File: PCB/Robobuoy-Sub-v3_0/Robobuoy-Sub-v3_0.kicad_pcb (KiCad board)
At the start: 2 copper layers, 141 parts, among them J201 Prog, J202 ESC_BB, J301 CHRG/DATA, J302 ESC_SB, J303 ESC_BB, J304 ESC_PWR_SB, J305 ESC_PWR_BB, J306 ACCU2, J307 ACCU2, Q201 MMBT3904, Q202 MMBT5401, Q203 MMBT5401, Q204 MMBT3904, Q205 AO3400A, Q301 AO3400A, Q302 AO3401A, Q303 AO3401A, Q304 AO3400A, Q305 AO3400A, Q306 HYG025N04NA1C2, Q307 HYG025N04NA1C2, SW201 ~{RESET}, SW202 MODE, SW301 On/Off, U201 LM1117S-3.3, U202 ESP32-WROOM-32E_(visible_peri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, U203 LSM303AGRTR, U301 SN74LV1T34DBV, U302 SN74LV1T34DBV, U303 LMR16020PDDA

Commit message: PCB changes
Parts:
- removed C225, C316: 100n, A_Device:C_0603
- removed C314: 100u/10V, Capacitor_SMD:C_1210_3225Metric
- removed C318: 4.7uF/10V, Capacitor_SMD:C_1206_3216Metric
- removed J307: ACCU2, A_Connector:AMASS_XT60IPW-M_1x03_P7.20mm_Horizontal
- removed Q307: HYG025N04NA1C2, Package_DFN_QFN:PQFN-8-EP_6x5mm_P1.27mm_Generic
- added H202: MountingHole, MountingHole:MountingHole_3.2mm_M3, F.Cu at (164.4, -60.3)
- added H203: MountingHole, MountingHole:MountingHole_3.2mm_M3, F.Cu at (164.4, -52.4)
- added H204: MountingHole, MountingHole:MountingHole_3.2mm_M3, F.Cu at (162.5, -74.5)
- added J203: ESC_BB, Connector_JST:JST_XH_B3B-XH-A_1x03_P2.50mm_Vertical, F.Cu at (128.1, -24.4)
- added Q308: AON6407-MS, Package_DFN_QFN:AO_DFN-8-1EP_5.55x5.2mm_P1.27mm_EP4.12x4.6mm, F.Cu at (31.4, 42.0)
- added R214: 100, A_Device:R_0603, F.Cu at (168.4, -77.3)
- C216, C218: value 1n -> 10n
- C217: value 10n -> 1n
- C219, C221: value 10n -> 100n
- C220: value 100n -> 10n
- C222: value 100n -> 100u/10V; footprint A_Device:C_0603 -> Capacitor_SMD:C_1210_3225Metric
- C223: value 100u/10V -> 1n; footprint Capacitor_SMD:C_1210_3225Metric -> A_Device:C_0603
- C224: value 1n -> 100n
- C308, C309: value 10u/25V -> 100n; footprint A_Device:C_0805 -> A_Device:C_0603
- C312: value 100n -> 1n
- C313: value 1n -> 100u/10V; footprint A_Device:C_0603 -> Capacitor_SMD:C_1210_3225Metric
- C315: value 100u/10V -> 100n; footprint Capacitor_SMD:C_1210_3225Metric -> A_Device:C_0603
- C317: value 100n -> 4.7uF/10V; footprint A_Device:C_0603 -> Capacitor_SMD:C_1206_3216Metric
- J202: value ESC_BB -> I2C; footprint Connector_JST:JST_XH_B3B-XH-A_1x03_P2.50mm_Vertical -> Connector_JST:JST_XH_B4B-XH-A_1x04_P2.50mm_Vertical
- J301: footprint A_Connector:AMASS_XT60IPW-M_1x03_P5.50mm_Vertical -> A_Connector:RoundWire_1x03_P5.50mm_Vertical
- J304, J305: footprint A_Connector:AMASS_XT60PW-F_1x02_P7.20mm_Horizontal -> Connector_AMASS:AMASS_XT30U-M_1x02_P5.0mm_Vertical
- J306: footprint A_Connector:AMASS_XT60IPW-M_1x03_P7.20mm_Horizontal -> Connector_AMASS:AMASS_XT30U-M_1x02_P5.0mm_Vertical
- Q306: value HYG025N04NA1C2 -> AON6407-MS; footprint Package_DFN_QFN:PQFN-8-EP_6x5mm_P1.27mm_Generic -> Package_DFN_QFN:AO_DFN-8-1EP_5.55x5.2mm_P1.27mm_EP4.12x4.6mm
- R208: value 100 -> 10K
- R209: value 10K -> 100
- R210: value 2.2k -> 10K
- R212: value 100 -> 2.2k
- moved C203 103.0 mm to (130.7, -73.9)
- moved C216 103.0 mm to (134.5, -73.9)
- moved C307 103.0 mm to (73.5, -73.9)
- moved R201 103.0 mm to (138.3, -73.9)
- moved R210 103.0 mm to (142.1, -73.9)
- moved R302 103.0 mm to (77.2, -73.9)
- moved TP302 103.0 mm to (63.2, -27.6)
- moved BZ201 103.0 mm to (115.2, -43.8)
- moved C201 103.0 mm to (130.7, -78.7)
- moved C202 103.0 mm to (130.7, -76.3)
- moved C204 103.0 mm to (130.7, -71.5)
- moved C205 103.0 mm to (133.2, -48.7)
- moved C206 103.0 mm to (133.2, -44.5)
- moved C207 103.0 mm to (130.7, -69.1)
- moved C208 103.0 mm to (133.2, -40.2)
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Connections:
- C216 pad 1: GND -> SWITCH
- C216 pad 2: /CPU/VSAMP -> +3.3V
- C217 pad 1: SWITCH -> GND
- C219 pad 1: GND -> +3.3V
- C219 pad 2: +3.3V -> GND
- C220 pad 1: +3.3V -> GND
- C220 pad 2: GND -> Net-(U203-VDD)
- C221 pad 1: GND -> Net-(U203-C1)
- C221 pad 2: Net-(U203-VDD) -> GND
- C222 pad 1: Net-(U203-C1) -> Net-(U203-VDD)
- C223 pad 1: Net-(U203-VDD) -> GND
- C223 pad 2: GND -> Net-(U203-VDD)
- C224 pad 1: GND -> Net-(U203-VDD)
- C224 pad 2: Net-(U203-VDD) -> GND
- C309 pad 1: Net-(D306-K) -> Net-(J302-Pin_2)
- C310 pad 1: Net-(J302-Pin_2) -> Net-(J303-Pin_2)
- C311 pad 1: Net-(J303-Pin_2) -> /Robobuoy-Sub-PSU-v3_0/buck_sw
- C311 pad 2: GND -> Net-(U303-BOOT)
- C312 pad 1: Net-(D307-K) -> +5V
- C312 pad 2: Net-(U303-BOOT) -> GND
- D307 pad 1: Net-(D307-K) -> /Robobuoy-Sub-PSU-v3_0/buck_sw
- J202 pad 1: +5V -> /CPU/SCL
- J202 pad 2: Net-(J202-Pin_2) -> /CPU/SDA
- J202 pad 3: GND -> +5V
- L301 pad 1: Net-(D307-K) -> /Robobuoy-Sub-PSU-v3_0/buck_sw
- Q306 pad 5: Net-(J304-Pin_2) -> Net-(J305-Pin_2)
- R208 pad 1: Net-(Q205-G) -> RX_SUB
- R208 pad 2: BUZZER -> +3.3V
- R209 pad 1: +3.3V -> Net-(Q205-G)
- R209 pad 2: SWITCH -> BUZZER
- R210 pad 2: Net-(U202-SDA/GPIO21) -> SWITCH
- R211 pad 2: Net-(U202-SCL/GPIO22) -> /CPU/SDA
- R212 pad 1: Net-(D202-DIN) -> +3.3V
- R212 pad 2: LEDS -> /CPU/SCL
- R213 pad 1: Net-(J202-Pin_2) -> Net-(D202-DIN)
- R213 pad 2: Net-(D204-DOUT) -> LEDS
- R325 pad 2: Net-(Q306-G) -> Net-(Q308-G)
- R326 pad 2: Net-(Q307-G) -> Net-(Q306-G)
- R327 pad 2: Net-(Q306-G) -> Net-(Q308-G)
- R328 pad 2: Net-(Q307-G) -> Net-(Q306-G)
- U202 pad 31: unconnected-(U202-MISO/GPIO19-Pad31) -> Net-(U202-MISO/GPIO19)
- U202 pad 33: Net-(U202-SDA/GPIO21) -> /CPU/SDA
- U202 pad 36: Net-(U202-SCL/GPIO22) -> /CPU/SCL
- U203 pad 1: Net-(U202-SCL/GPIO22) -> /CPU/SCL
- U203 pad 11: unconnected-(U203-DRDY_MAG-Pad11) -> Net-(U202-MISO/GPIO19)
- U203 pad 4: Net-(U202-SDA/GPIO21) -> /CPU/SDA
- U303 pad 8: Net-(D307-K) -> /Robobuoy-Sub-PSU-v3_0/buck_sw
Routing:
- net GND: track 0.00 -> 127.2 mm, vias 0 -> 19
- net Vbatt: track 0.00 -> 58.1 mm
- net Net-(J302-Pin_2): track 0.00 -> 21.6 mm
- net Net-(J303-Pin_2): track 0.00 -> 17.5 mm
- net Net-(J303-Pin_1): track 0.00 -> 17.1 mm
- net Net-(Q306-G): track 0.00 -> 13.4 mm, vias 0 -> 2
- net Net-(J302-Pin_1): track 0.00 -> 11.6 mm
- net Net-(J305-Pin_2): track 0.00 -> 7.07 mm
- net Net-(J304-Pin_2): track 0.00 -> 7.07 mm
- net Net-(U303-FB): track 0.00 -> 5.04 mm
- net Net-(U301-A): track 0.00 -> 3.41 mm
- net Net-(U302-A): track 0.00 -> 3.21 mm
- net /Robobuoy-Sub-PSU-v3_0/buck_sw: track 0.00 -> 3.17 mm
- net Net-(U303-BOOT): track 0.00 -> 2.67 mm
- net Net-(Q305-D): track 0.00 -> 1.98 mm
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- added copper zone on F.Cu, net +5V
- added copper zone on F.Cu, net /Robobuoy-Sub-PSU-v3_0/buck_sw
- added copper zone on F.Cu, net GND
- added copper zone on In1.Cu, net GND
- added copper zone on In2.Cu, net GND
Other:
- board outline added: 112 x 66 mm
- copper layers 2 -> 4

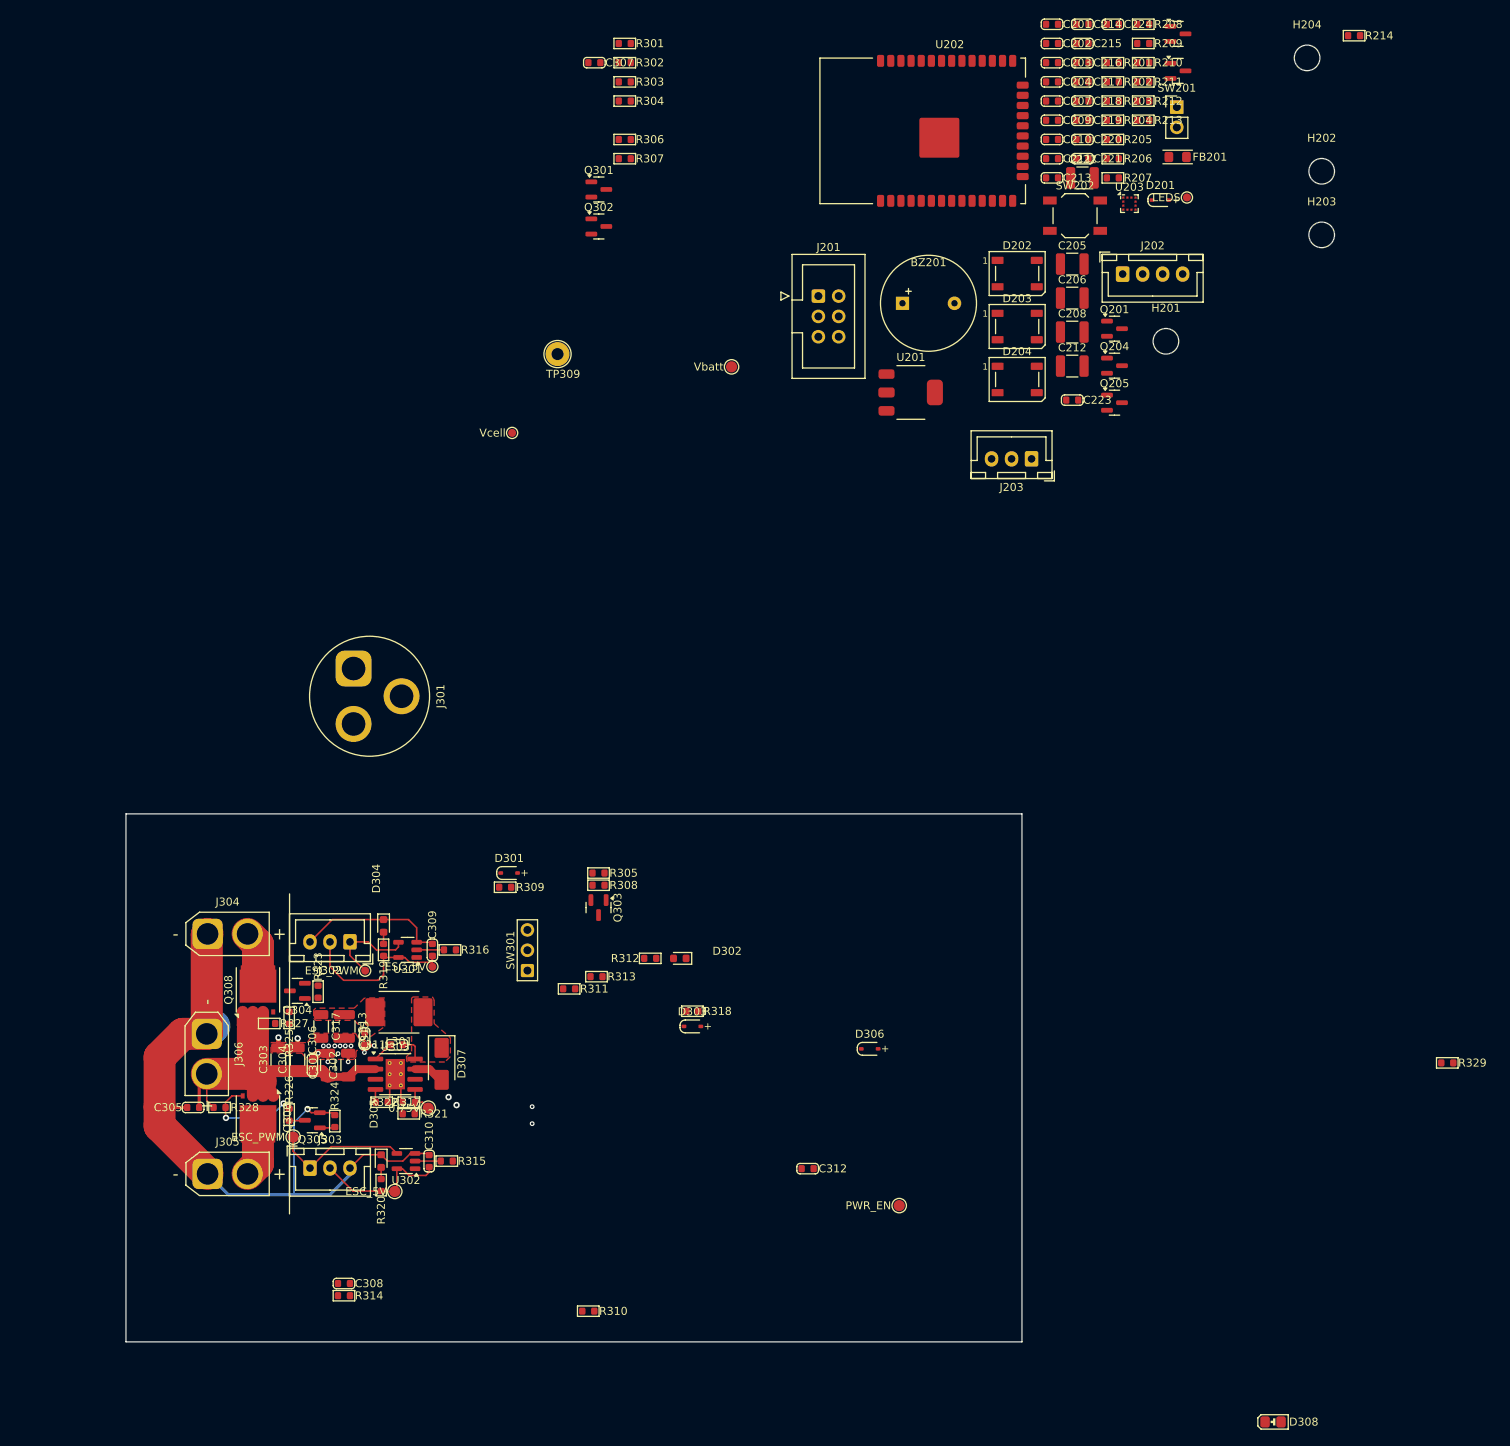
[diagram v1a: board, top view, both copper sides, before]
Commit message: PCB 3.0 almoste finished Imon calculation added
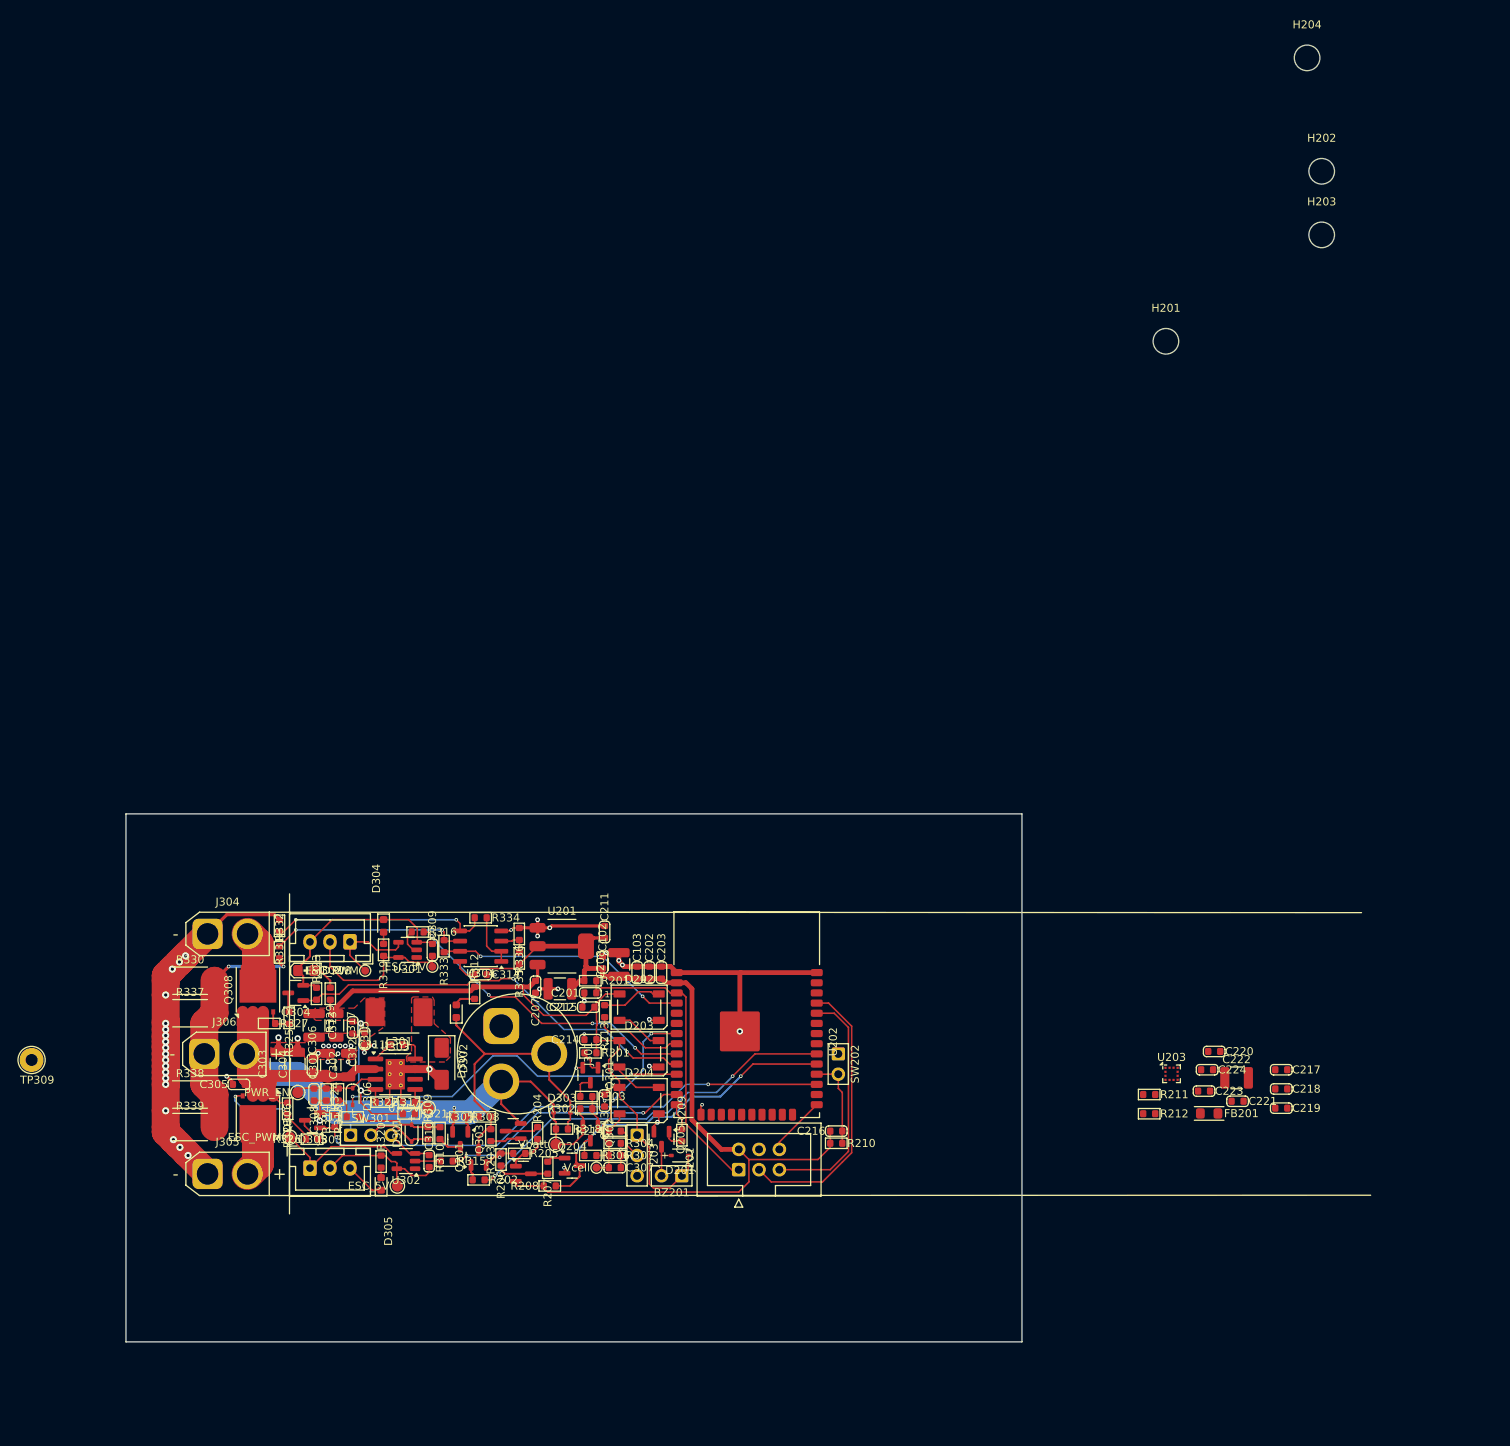
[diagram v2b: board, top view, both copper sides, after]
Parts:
- removed C204, C209, C210: 100n, A_Device:C_0603
- removed C205, C206: 100u/10V, Capacitor_SMD:C_1210_3225Metric
- removed J202: I2C, Connector_JST:JST_XH_B4B-XH-A_1x04_P2.50mm_Vertical
- removed SW201: ~{RESET}, Connector_PinHeader_2.54mm:PinHeader_1x02_P2.54mm_Vertical
- removed TP201: LEDS, A_Pads_Pins:Testpad_1
- added C102: 100n, A_Device:C_0603, F.Cu at (74.5, 38.6)
- added C103: 100n, A_Device:C_0603, F.Cu at (78.8, 39.8)
- added C314: 100n, A_Device:C_0603, F.Cu at (59.2, 40.1)
- added R330: 1, Resistor_SMD:R_2512_6332Metric_Pad1.40x3.35mm_HandSolder, F.Cu at (22.9, 40.9)
- added R331: 1.5K, A_Device:R_0603, F.Cu at (34.1, 34.0)
- added R332: 1.5K, A_Device:R_0603, F.Cu at (34.1, 37.3)
- added R333: 4.6K, A_Device:R_0603, F.Cu at (54.7, 36.5)
- added R334: 4.6K, A_Device:R_0603, F.Cu at (59.2, 33.0)
- added R335: 10K, A_Device:R_0603, F.Cu at (64.1, 38.1)
- added R336: 10K, A_Device:R_0603, F.Cu at (64.1, 35.0)
- added R337: 1, Resistor_SMD:R_2512_6332Metric_Pad1.40x3.35mm_HandSolder, F.Cu at (22.9, 44.9)
- added R338: 1, Resistor_SMD:R_2512_6332Metric_Pad1.40x3.35mm_HandSolder, F.Cu at (22.9, 55.1)
- added R339: 1, Resistor_SMD:R_2512_6332Metric_Pad1.40x3.35mm_HandSolder, F.Cu at (22.9, 59.1)
- added U304: TL082, Package_SO:SO-8_3.9x4.9mm_P1.27mm, F.Cu at (59.2, 36.5)
- BZ201: footprint A_Misc:Buzzer-12x6.5x5.2 -> A_Connector:Header_1x02_P2.54_Jumper
- J203: footprint Connector_JST:JST_XH_B3B-XH-A_1x03_P2.50mm_Vertical -> A_Connector:Header_1x03_P2.54_Male
- SW202: footprint Button_Switch_SMD:SW_SPST_TL3342 -> A_Connector:Header_1x02_P2.54_Jumper
- moved R214 165.2 mm to (76.0, 59.7), turned to 180 degrees
- moved R208 163.1 mm to (67.9, 66.5), turned to 180 degrees
- moved Q202 160.4 mm to (63.3, 59.7), turned to 180 degrees
- moved Q203 160.3 mm to (64.6, 65.0)
- moved R202 158.5 mm to (59.0, 65.7)
- moved R203 150.8 mm to (60.5, 60.2), turned to -90 degrees
- moved R209 148.1 mm to (84.4, 60.2), turned to 90 degrees
- moved R205 146.9 mm to (64.1, 62.4)
- moved R206 146.6 mm to (61.8, 63.2), turned to -90 degrees
- moved R204 145.6 mm to (66.3, 59.9), turned to 90 degrees
- moved R207 142.5 mm to (67.6, 64.2), turned to -90 degrees
- moved C214 141.0 mm to (73.0, 48.2), turned to 180 degrees
- moved R210 140.4 mm to (103.7, 61.2)
- moved R329 139.9 mm to (40.4, 42.5), turned to -90 degrees
- moved C307 138.1 mm to (76.0, 64.2)
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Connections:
- J306 pad 1: GND -> GND1
- U202 pad 10: /CPU/ESC_BB -> /CPU/ESC_SB_PWR
- U202 pad 13: /CPU/ESC_SB -> /CPU/ESC_BB
- U202 pad 16: LEDS -> unconnected-(U202-MTCK/MOSI/D3/GPIO13-Pad16)
- U202 pad 26: /CPU/ESC_SB_PWR -> unconnected-(U202-D1/GPIO4-Pad26)
- U202 pad 28: unconnected-(U202-TXD/GPIO17-Pad28) -> SWITCH
- U202 pad 4: unconnected-(U202-GPIO36-Pad4) -> /CPU/Imon
- U202 pad 8: SWITCH -> LEDS
- U202 pad 9: unconnected-(U202-GPIO33-Pad9) -> /CPU/ESC_SB
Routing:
- net +3.3V: track 0.00 -> 114.2 mm
- net +5V: track 0.00 -> 102.8 mm, vias 0 -> 2
- net /CPU/ESC_BB_PWR: track 1.90 -> 67.2 mm, vias 0 -> 2
- net GND: track 127.2 -> 187.4 mm, vias 19 -> 58
- net Vbatt: track 58.1 -> 116.6 mm, vias 0 -> 1
- net /CPU/ESC_SB_PWR: track 0.00 -> 52.2 mm, vias 0 -> 2
- net TX_SUB: track 0.00 -> 48.0 mm, vias 0 -> 2
- net /CPU/ON: track 0.00 -> 44.8 mm, vias 0 -> 2
- net RX_SUB: track 0.00 -> 41.4 mm, vias 0 -> 2
- net /Robobuoy-Sub-PSU-v3_0/COMM: track 0.00 -> 39.0 mm
- net EN: track 0.00 -> 38.3 mm
- net /CPU/ESC_SB: track 0.00 -> 38.1 mm, vias 0 -> 4
- net TX: track 0.00 -> 35.1 mm
- net /CPU/Imon: track 0.00 -> 31.8 mm, vias 0 -> 2
- net /CPU/ESC_BB: track 0.00 -> 31.4 mm, vias 0 -> 2
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
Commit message: pcb ready for production
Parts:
- removed C217, C223: 1n, A_Device:C_0603
- removed C218, C220: 10n, A_Device:C_0603
- removed C219, C221, C224: 100n, A_Device:C_0603
- removed C222: 100u/10V, Capacitor_SMD:C_1210_3225Metric
- removed FB201: 0.3E 240E@100MHz, A_Device:L_0805_(1.2)
- removed TP309: GND, TestPoint:TestPoint_Loop_D2.54mm_Drill1.5mm_Beaded
- removed U203: LSM303AGRTR, A_Device:LGA-12_2x2mm_P0.5mm
- added C113: 100n, A_Device:C_0603, F.Cu at (116.6, 48.7)
- added C114: 1u/50V, A_Device:C_0603, F.Cu at (116.6, 45.9)
- added C115: 10n, A_Device:C_0603, F.Cu at (114.1, 44.9)
- added C116: 100n, A_Device:C_0603, F.Cu at (112.3, 47.5)
- added C124: 1n, A_Device:C_0603, F.Cu at (114.4, 49.5)
- added C401: 1u/50V, A_Device:C_0603, F.Cu at (110.3, 57.6)
- added C402: 1u/50V, A_Device:C_0603, F.Cu at (110.5, 63.5)
- added C403: 100n, A_Device:C_0603, F.Cu at (113.3, 66.0)
- added C404: 10n, A_Device:C_0603, F.Cu at (111.8, 66.0)
- added C405: 100n, A_Device:C_0603, F.Cu at (116.4, 66.0)
- added C406: 10n, A_Device:C_0603, F.Cu at (117.7, 62.4)
- added J102: Display, A_Connector:Header_1x04_P2.54_Male, F.Cu at (110.3, 50.0)
- added J401: Display, A_Connector:Header_1x04_P2.54_Male, F.Cu at (104.7, 50.0)
- added Q401: AO3400A, Package_TO_SOT_SMD:SOT-23, F.Cu at (114.1, 55.1)
- added Q403: AO3400A, Package_TO_SOT_SMD:SOT-23, F.Cu at (117.7, 55.1)
- added R105: 10K, A_Device:R_0603, F.Cu at (117.7, 57.9)
- added R401: 10K, A_Device:R_0603, F.Cu at (116.4, 52.8)
- added R402: 10K, A_Device:R_0603, F.Cu at (114.1, 57.9)
- added R403: 10K, A_Device:R_0603, F.Cu at (112.8, 52.8)
- added R404: 10K, A_Device:R_0603, F.Cu at (114.9, 66.0)
- added U102: LSM303AGRTR, A_Device:LGA-12_2x2mm_P0.5mm, F.Cu at (114.4, 47.5)
- added U401: LP5907MFX-1.8, Package_TO_SOT_SMD:SOT-23-5, F.Cu at (110.5, 60.5)
- added U403: ICM-20948, Sensor_Motion:InvenSense_QFN-24_3x3mm_P0.4mm, F.Cu at (114.9, 62.2)
- J306: value ACCU2 -> LiPo S6
- moved R212 42.7 mm to (103.2, 41.6), turned to -90 degrees
- moved R211 40.4 mm to (104.7, 41.6), turned to -90 degrees
- moved SW202 10.2 mm to (104.5, 61.4)
- moved C305 8.02 mm to (34.2, 47.7), turned to 0 degrees
- moved C216 5.14 mm to (104.5, 64.7)
- moved R210 5.14 mm to (104.5, 66.3)
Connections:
- J306 pad 1: GND1 -> Net-(J306--)
- R330 pad 2: GND1 -> Net-(J306--)
- R331 pad 1: GND -> Net-(J306--)
- R332 pad 1: GND1 -> GND
- R337 pad 2: GND1 -> Net-(J306--)
- R338 pad 2: GND1 -> Net-(J306--)
- R339 pad 2: GND1 -> Net-(J306--)
- U202 pad 31: Net-(U202-MISO/GPIO19) -> unconnected-(U202-MISO/GPIO19-Pad31)
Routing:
- net GND: track 187.4 -> 327.9 mm, vias 58 -> 135
- net +3.3V: track 114.2 -> 194.4 mm, vias 0 -> 2
- net /CPU/SDA: track 0.00 -> 36.2 mm, vias 0 -> 2
- net Net-(J306--): track 0.00 -> 34.5 mm
- net /CPU/SCL: track 0.00 -> 31.1 mm, vias 0 -> 3
- net GND1: track 30.0 -> 0.00 mm, vias 2 -> 0
- net +1.8V: track 0.00 -> 29.5 mm
- net TX: track 35.1 -> 24.6 mm, vias 0 -> 1
- net SCL_LV: track 0.00 -> 8.33 mm
- net Net-(J304-Pin_2): track 7.07 -> 14.2 mm, vias 0 -> 12
- net Net-(J305-Pin_2): track 7.07 -> 14.2 mm, vias 0 -> 12
- net RX: track 29.8 -> 23.7 mm, vias 0 -> 1
- net SDA_LV: track 0.00 -> 5.17 mm
- net SWITCH: track 11.5 -> 15.7 mm
- net Vbatt: track 116.6 -> 120.6 mm
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- added copper zone on B.Cu, net GND
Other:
- board size 112 x 66 mm -> 103 x 36 mm
